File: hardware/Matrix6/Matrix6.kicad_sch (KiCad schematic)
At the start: 32 parts, among them J1 USB4105-GF-A-120, J2 GPIO / POWER, J3 GPIO / POWER, SW1 RESET, SW2 BOOT, U1 ESP32-S3-WROOM-1-N8R8, U2 AP63203WU-7, U3 USBLC6-2SC6

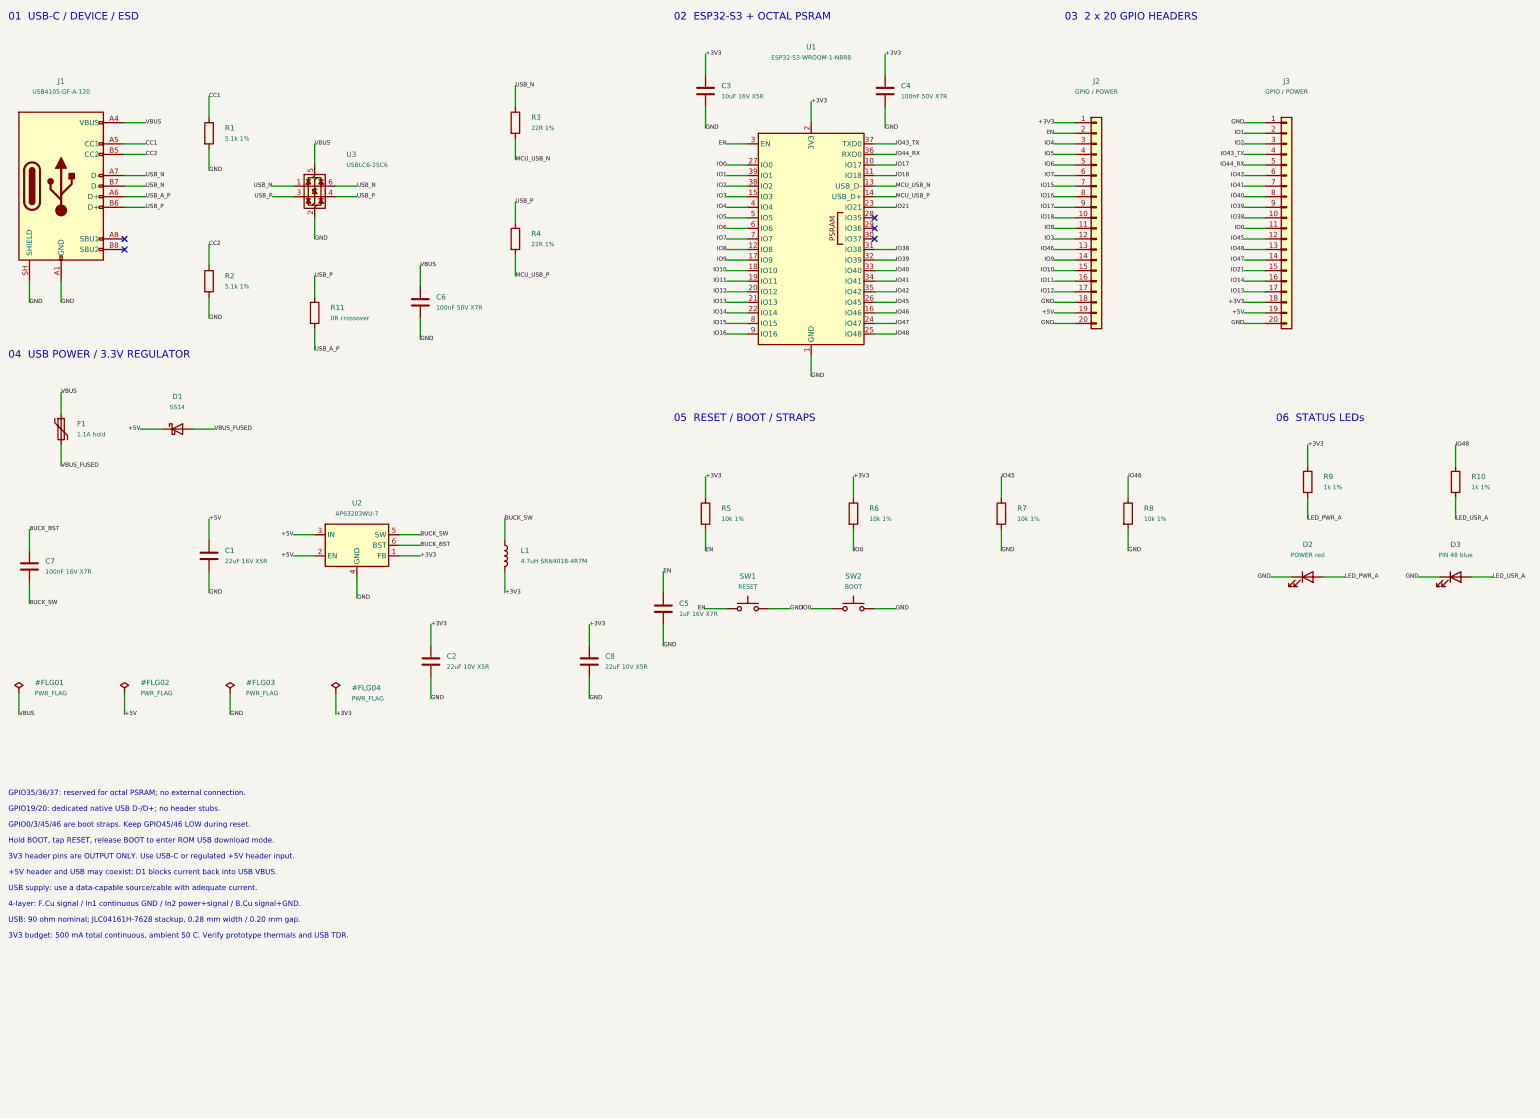
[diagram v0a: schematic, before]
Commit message: Align Matrix6 v0.5 headers and manual routing with Matrix5 shields
Use two 20-pin sockets at 33.02 mm spacing and remap the GPIO and power nets against Matrix5 Main and all eleven shield designs. Document the three unused USB/VBAT pins, fused VBUS output and prototype power/mechanical limits.

Preserve the reviewed USB copper, connector body keepout, continuous L2 GND and design rules. Include schematic/PCB/3D previews and reproducible DRC, ERC, pin-map, keepout and electrical checks; all current DRC/ERC/parity/unconnected checks pass.
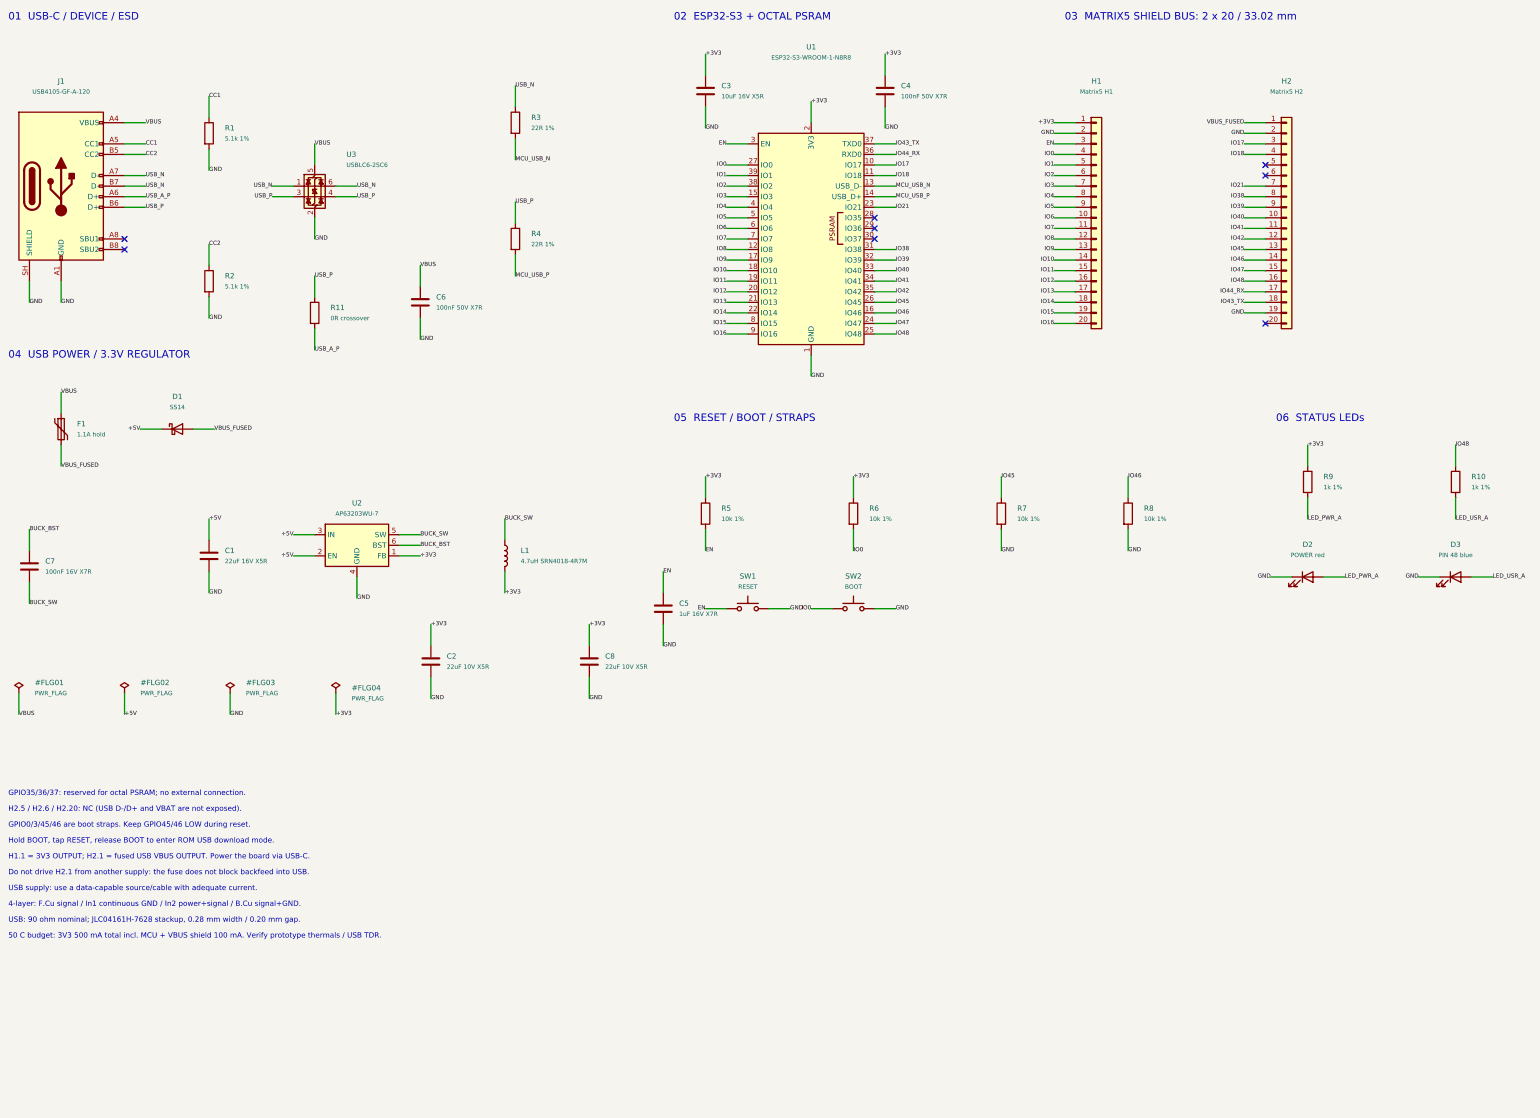
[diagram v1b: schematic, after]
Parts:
- H1: renamed from J2; value GPIO / POWER -> Matrix5 H1; footprint Connector_PinHeader_2.54mm:PinHeader_1x20_P2.54mm_Vertical -> Connector_PinSocket_2.54mm:PinSocket_1x20_P2.54mm_Vertical
- H2: renamed from J3; value GPIO / POWER -> Matrix5 H2; footprint Connector_PinHeader_2.54mm:PinHeader_1x20_P2.54mm_Vertical -> Connector_PinSocket_2.54mm:PinSocket_1x20_P2.54mm_Vertical
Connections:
- net +3V3: no longer H2.18 (Pin_18)
- net +5V: no longer H1.19 (Pin_19), H2.19 (Pin_19)
- net EN: now also H1.3 (Pin_3); no longer H1.2 (Pin_2)
- net GND: now also H1.2 (Pin_2), H2.19 (Pin_19), H2.2 (Pin_2); no longer H1.18 (Pin_18), H1.20 (Pin_20), H2.1 (Pin_1), H2.20 (Pin_20)
- net IO0: now also H1.4 (Pin_4); no longer H2.11 (Pin_11)
- net IO1: now also H1.5 (Pin_5); no longer H2.2 (Pin_2)
- net IO10: now also H1.14 (Pin_14); no longer H1.15 (Pin_15)
- net IO11: now also H1.15 (Pin_15); no longer H1.16 (Pin_16)
- net IO12: now also H1.16 (Pin_16); no longer H1.17 (Pin_17)
- net IO13: now also H1.17 (Pin_17); no longer H2.17 (Pin_17)
- net IO14: now also H1.18 (Pin_18); no longer H2.16 (Pin_16)
- net IO15: now also H1.19 (Pin_19); no longer H1.7 (Pin_7)
- net IO16: now also H1.20 (Pin_20); no longer H1.8 (Pin_8)
- net IO17: now also H2.3 (Pin_3); no longer H1.9 (Pin_9)
- net IO18: now also H2.4 (Pin_4); no longer H1.10 (Pin_10)
- net IO2: now also H1.6 (Pin_6); no longer H2.3 (Pin_3)
- net IO21: now also H2.7 (Pin_7); no longer H2.15 (Pin_15)
- net IO3: now also H1.7 (Pin_7); no longer H1.12 (Pin_12)
- net IO38: now also H2.8 (Pin_8); no longer H2.10 (Pin_10)
- net IO4: now also H1.8 (Pin_8); no longer H1.3 (Pin_3)
- net IO40: now also H2.10 (Pin_10); no longer H2.8 (Pin_8)
- net IO41: now also H2.11 (Pin_11); no longer H2.7 (Pin_7)
- net IO42: now also H2.12 (Pin_12); no longer H2.6 (Pin_6)
- net IO43_TX: now also H2.18 (Pin_18); no longer H2.4 (Pin_4)
- net IO44_RX: now also H2.17 (Pin_17); no longer H2.5 (Pin_5)
- net IO45: now also H2.13 (Pin_13); no longer H2.12 (Pin_12)
- net IO46: now also H2.14 (Pin_14); no longer H1.13 (Pin_13)
- net IO47: now also H2.15 (Pin_15); no longer H2.14 (Pin_14)
- net IO48: now also H2.16 (Pin_16); no longer H2.13 (Pin_13)
- net IO5: now also H1.9 (Pin_9); no longer H1.4 (Pin_4)
- net IO6: now also H1.10 (Pin_10); no longer H1.5 (Pin_5)
- net IO7: now also H1.11 (Pin_11); no longer H1.6 (Pin_6)
- net IO8: now also H1.12 (Pin_12); no longer H1.11 (Pin_11)
- net IO9: now also H1.13 (Pin_13); no longer H1.14 (Pin_14)
- net VBUS_FUSED: now also H2.1 (Pin_1)
- no-connect marks 5 -> 8
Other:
- note added: "03 MATRIX5 SHIELD BUS: 2 x 20 / 33.02 mm"
- note added: "50 C budget: 3V3 500 mA total incl. MCU + VBUS shield 100 mA. Verify prototype thermals / USB TDR."
- note added: "Do not drive H2.1 from another supply: the fuse does not block backfeed into USB."
- note added: "H1.1 = 3V3 OUTPUT; H2.1 = fused USB VBUS OUTPUT. Power the board via USB-C."
- note added: "H2.5 / H2.6 / H2.20: NC (USB D-/D+ and VBAT are not exposed)."
- note removed: "+5V header and USB may coexist: D1 blocks current back into USB VBUS."
- note removed: "03 2 x 20 GPIO HEADERS"
- note removed: "3V3 budget: 500 mA total continuous, ambient 50 C. Verify prototype thermals and USB TDR."
- note removed: "3V3 header pins are OUTPUT ONLY. Use USB-C or regulated +5V header input."
- note removed: "GPIO19/20: dedicated native USB D-/D+; no header stubs."
- title: ESP32-S3 DevBoard | Native USB-C -> Matrix6 - ESP32-S3 / Matrix5 shield interface

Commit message: Add rear microSD with clear extraction path and LiPo power to Matrix Six
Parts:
- removed U2: AP63203WU-7, Package_TO_SOT_SMD:TSOT-23-6, symbol Regulator_Switching:AP63203WU
- added C10, C11, C9: 22uF 25V X5R, Capacitor_SMD:C_0805_2012Metric, symbol Device:C
- added C12: 100nF, Capacitor_SMD:C_0603_1608Metric, symbol Device:C
- added J2: microSD (rear), Connector_Card:microSD_HC_Hirose_DM3AT-SF-PEJM5, symbol Connector:Micro_SD_Card_Det_Hirose_DM3AT
- added J3: LiPo 1S / PH2, Connector_JST:JST_PH_S2B-PH-K_1x02_P2.00mm_Horizontal, symbol Connector_Generic:Conn_01x02
- added Q1: AO3401A, Package_TO_SOT_SMD:SOT-23, symbol Transistor_FET:AO3401A
- added R12: 100R, Resistor_SMD:R_0603_1608Metric, symbol Device:R
- added R13: 10k / 100mA, Resistor_SMD:R_0603_1608Metric, symbol Device:R
- added R14: 100k, Resistor_SMD:R_0603_1608Metric, symbol Device:R
- added R15, R16, R17, R18, R19: 10k, Resistor_SMD:R_0603_1608Metric, symbol Device:R
- added U2: TPS63001 (3.3V), Package_SON:Texas_DRC0010J, symbol Regulator_Switching:TPS63001
- added U4: MCP73831 / 100mA, Package_TO_SOT_SMD:SOT-23-5, symbol Battery_Management:MCP73831-2-OT
- C1: value 22uF 16V X5R -> 22uF 25V X5R; LCSC (none) -> C45783; MPN (none) -> CL21A226MAQNNNE
- C2, C8: value 22uF 10V X5R -> 22uF 25V X5R; LCSC (none) -> C45783; MPN (none) -> CL21A226MAQNNNE
- C7: value 100nF 16V X7R -> 100nF
- L1: value 4.7uH SRN4018-4R7M -> 2.2uH / 3A; LCSC (none) -> C913207; MPN (none) -> SRN4018-2R2M
- R7: value 10k 1% -> 10k; LCSC (none) -> C25804; MPN (none) -> 0603WAF1002T5E
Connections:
- net +3V3: now also C11.1, C12.1, J2.4 (VDD), R15.2, R16.2, R17.2, R18.2, R19.2, U2.1 (VOUT), U2.10 (FB); no longer L1.2
- net GND: now also C7.2, C10.2, C11.2, C12.2, C9.2, J2.6 (VSS), J2.SH (SHIELD), J3.2 (Pin_2), R13.2, R14.2, U2.11 (PGND), U2.3 (PGND), U2.7 (PS/SYNC), U2.9 (GND), U4.2 (V_{SS})
- net IO10: now also J2.2 (DAT3/CD), R16.1
- net IO11: now also J2.3 (CMD), R17.1
- net IO12: now also J2.5 (CLK)
- net IO13: now also J2.7 (DAT0), R18.1
- net VBUS_FUSED: now also C9.1, Q1.1 (G), R14.1, U4.4 (V_{DD})
- net VBAT: now reaches H2.20 (Pin_20)
- net VBAT: now also C10.1, J3.1 (Pin_1), Q1.3 (D), U4.3 (V_{BAT})
- net +5V renamed VSYS
- net VSYS: now also Q1.2 (S), R12.1, U2.5 (VIN), U2.6 (EN)
- net BUCK_BST renamed VINA
- net VINA: now also R12.2, U2.8 (VINA)
- net BUCK_SW renamed SW_L1
- net SW_L1: now also U2.4 (L1); no longer C7.2
- new net CHG_PROG: R13.1, U4.5 (PROG)
- new net SD_DAT1: J2.8 (DAT1), R19.1
- new net SD_DAT2: J2.1 (DAT2), R15.1
- new net SW_L2: L1.2, U2.2 (L2)
- no-connect marks 8 -> 10
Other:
- note added: "04 USB / BATTERY TO REGULATED 3.3V"
- note added: "07 REAR microSD / MATRIX5 SPI"
- note added: "08 1S LiPo / USB CHARGING / AUTOMATIC SOURCE SELECTION"
- note added: "100mA charge; >=500mAh, >=1A discharge. No cell temperature sensor."
- note added: "3V3 budget: 500mA total including MCU, SD and shields. Prototype load / thermal / USB TDR tests required."
- note added: "Designed By GPT-6 Astra"
- note added: "H2.20 = VBAT. H2.1 = fused USB output; no 5V output on battery."
- note added: "J3: pin 1 = BAT+, pin 2 = GND. Use a protected 3.7V / 4.2V pack."
- note added: "SD opening faces the antenna edge. Keep rear card withdrawal corridor clear."
- note added: "SD shares shield SPI pins. Remove card for conflicting GPIO / I2C use."
- note added: "SD: CS=10, MOSI=11, CLK=12, MISO=13; 20MHz maximum bring-up."
- note removed: "04 USB POWER / 3.3V REGULATOR"
- note removed: "4-layer: F.Cu signal / In1 continuous GND / In2 power+signal / B.Cu signal+GND."
- note removed: "50 C budget: 3V3 500 mA total incl. MCU + VBUS shield 100 mA. Verify prototype thermals / USB TDR."
- note removed: "Do not drive H2.1 from another supply: the fuse does not block backfeed into USB."
- note removed: "GPIO0/3/45/46 are boot straps. Keep GPIO45/46 LOW during reset."
- note removed: "GPIO35/36/37: reserved for octal PSRAM; no external connection."
- note removed: "H1.1 = 3V3 OUTPUT; H2.1 = fused USB VBUS OUTPUT. Power the board via USB-C."
- note removed: "H2.5 / H2.6 / H2.20: NC (USB D-/D+ and VBAT are not exposed)."
- note removed: "Hold BOOT, tap RESET, release BOOT to enter ROM USB download mode."
- note removed: "USB supply: use a data-capable source/cable with adequate current."
- note removed: "USB: 90 ohm nominal; JLC04161H-7628 stackup, 0.28 mm width / 0.20 mm gap."
- title: Matrix6 - ESP32-S3 / Matrix5 shield interface -> Matrix Six - ESP32-S3 / microSD / LiPo
